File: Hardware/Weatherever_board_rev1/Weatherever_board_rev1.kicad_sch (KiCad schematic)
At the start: 44 parts, among them J101 USB_B_Micro, J102 Expansion conn, J103 DebugConn, U101 USBLC6-2P6, U102 FT230XQ, U103 AOZ1312, U104 NCP115AMX250TCG, U105 STM32G030C8T6, U106 M24C08-W, U107 M24C08-W, Y101 49S-16.000MEEJ-T 16MHz, Y102 32.768K-CFPX217

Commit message: Finished HW schematic and minor project cleanup
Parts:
- removed R108: 2k, Resistor_SMD:R_0805_2012Metric_Pad1.20x1.40mm_HandSolder, symbol Device:R_Small
- added C104: 10u, Capacitor_SMD:C_0805_2012Metric_Pad1.18x1.45mm_HandSolder, symbol Device:C_Small
- added D101: ERR_LED (RED), symbol Device:LED
- added J103: Test pins COMM1, Connector_PinHeader_2.54mm:PinHeader_2x03_P2.54mm_Vertical, symbol Connector_Generic:Conn_01x06
- added J105: Test pins Probe, Connector_PinHeader_2.54mm:PinHeader_1x02_P2.54mm_Vertical, symbol Connector_Generic:Conn_01x02
- added J106: Test pins COMM2, Connector_PinHeader_2.54mm:PinHeader_2x03_P2.54mm_Vertical, symbol Connector_Generic:Conn_01x06
- added R101, R102: 2k, Resistor_SMD:R_0805_2012Metric_Pad1.20x1.40mm_HandSolder, symbol Device:R_Small
- added R103: 270, Resistor_SMD:R_0805_2012Metric_Pad1.20x1.40mm_HandSolder, symbol Device:R_Small
- added R109, R110: 3k3, Resistor_SMD:R_0805_2012Metric_Pad1.20x1.40mm_HandSolder, symbol Device:R_Small
- added SW101: DBG - Normal, symbol Switch:SW_DIP_x01
- added SW102: RESET, symbol Switch:SW_MEC_5E
- R111: renamed from R106; value 2k -> 3k3
- R112: renamed from R107; value 2k -> 3k3
- renumbered C104 to C105, C105 to C106, C106 to C107, C107 to C108, C108 to C109, C109 to C110, C110 to C111, C111 to C112, C112 to C113, C113 to C114, C114 to C115, D101 to D102, D102 to D103, J103 to J104, R101 to R104, R102 to R105, R103 to R106, R104 to R107, R105 to R108, R109 to R113, R110 to R114
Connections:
- net +3V3: now also U106.3 (E2), R101.2, R102.1, R103.1, R109.1, R110.1
- net GNDD: now also U106.7 (WC), U107.3 (E2), U107.7 (WC), C104.2, J103.6 (Pin_6), J105.2 (Pin_2), J106.6 (Pin_6), SW101.1, SW102.1, SW102.2
- net I2C1_SCL: now also R111.2
- net I2C1_SDA: now also R112.2
- net I2C2_SCL_MEM: now also R109.2, R110.2; no longer R111.2
- net I2C2_SDA_MEM: no longer R112.2
- net SPI1_CS1: now also J103.2 (Pin_2)
- net SPI1_CS2: now also J103.1 (Pin_1)
- net SPI1_MISO: now also J103.4 (Pin_4)
- net SPI1_MOSI: now also J103.3 (Pin_3)
- net SPI1_SCK: now also J103.5 (Pin_5)
- net TIM_IN: now also J105.1 (Pin_1)
- net USART1_CTS: now also J106.4 (Pin_4)
- net USART1_RTS: now also J106.3 (Pin_3)
- net USART1_RX: now also J106.2 (Pin_2)
- net USART1_TX: now also J106.1 (Pin_1)
- net USB_D+: now also J101.3 (D+); no longer U102.6 (USBDP)
- net USB_D-: now also J101.2 (D-), U101.6 (I/O1); no longer U101.3 (I/O2), U102.7 (USBDM)
- net USB_D_S-: now reaches U101.1 (I/O1)
- net USB_D_S-: now also U102.7 (USBDM); no longer J101.2 (D-)
- net ~{RESET}: now reaches U105.10 (NRST)
- net ~{RESET}: now also C104.1, R102.2, SW102.3 (K), SW102.4 (A)
- net ~{ERR_LED}: now reaches U105.40 (PD2)
- net ~{ERR_LED}: now also D101.1 (K)
- net OVERTEMP_INT: now reaches U105.41 (PD3)
- net MODE_SEL: now reaches U105.42 (PB3)
- net MODE_SEL: now also R101.1, SW101.2
- new net: D101.2 (A), R103.2
- new net USB_D_S+: U101.3 (I/O2), U102.6 (USBDP)
- no-connect marks 22 -> 20
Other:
- added sheet OnBoardThermometer (OnBoardThermometer.kicad_sch)
- note added: "Device I^{2}C address: 0x50"
- note added: "Device I^{2}C address: 0x54"
- note added: "Error indicator LED and RESET button"
- note added: "Mode select switch"
- note added: "SW ON -> Debug SW OFF -> Normal"
- note added: "The _S suffix is for "Safe" (from ESD threats :))"
- moved on the sheet: C109, J101, J102, R111, R112, U101, U106

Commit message: Funished schematics and GPIO drv interface
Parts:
- removed R113, R114: 10k, Resistor_SMD:R_0805_2012Metric_Pad1.20x1.40mm_HandSolder, symbol Device:R_Small
- added J107: Test pins I2C, Connector_PinHeader_2.54mm:PinHeader_2x03_P2.54mm_Vertical, symbol Connector_Generic:Conn_01x06
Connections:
- net GNDD: now also J107.3 (Pin_3), J107.4 (Pin_4)
- net I2C1_SCL: now also J107.5 (Pin_5)
- net I2C1_SDA: now also J107.6 (Pin_6)
- net I2C2_SCL_MEM: now also J107.1 (Pin_1)
- net I2C2_SDA_MEM: now also J107.2 (Pin_2)
- net RF_DIO_2: now reaches U105.23 (PB11)
- net RF_DIO_3: now reaches U105.24 (PB12)
- net RF_DIO_5: now reaches U105.43 (PB4)
- net RF_DIO_4: now reaches U105.44 (PB5)
- net OVERTEMP_INT renamed PRS_RDY
- net RF_GDO0 renamed RF_DIO_0
- net RF_GDO2 renamed RF_DIO_1
- no-connect marks 20 -> 16
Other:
- sheet OnBoardThermometer renamed EvnSensors
- added sheet USB_Dongle (USB_Dongle.kicad_sch)
- sheet EvnSensors ports: added PREASURE_IRQ, SCL_SENS, SDA_SENS; removed OVERTEMP_THM, SCL_THM, SDA_THM
- sheet RadioComm ports: added RF_DIO0, RF_DIO1, RF_DIO2, RF_DIO3, RF_DIO4, RF_DIO5, RF_RESET; removed RF_GDO0, RF_GDO2
- moved on the sheet: J105

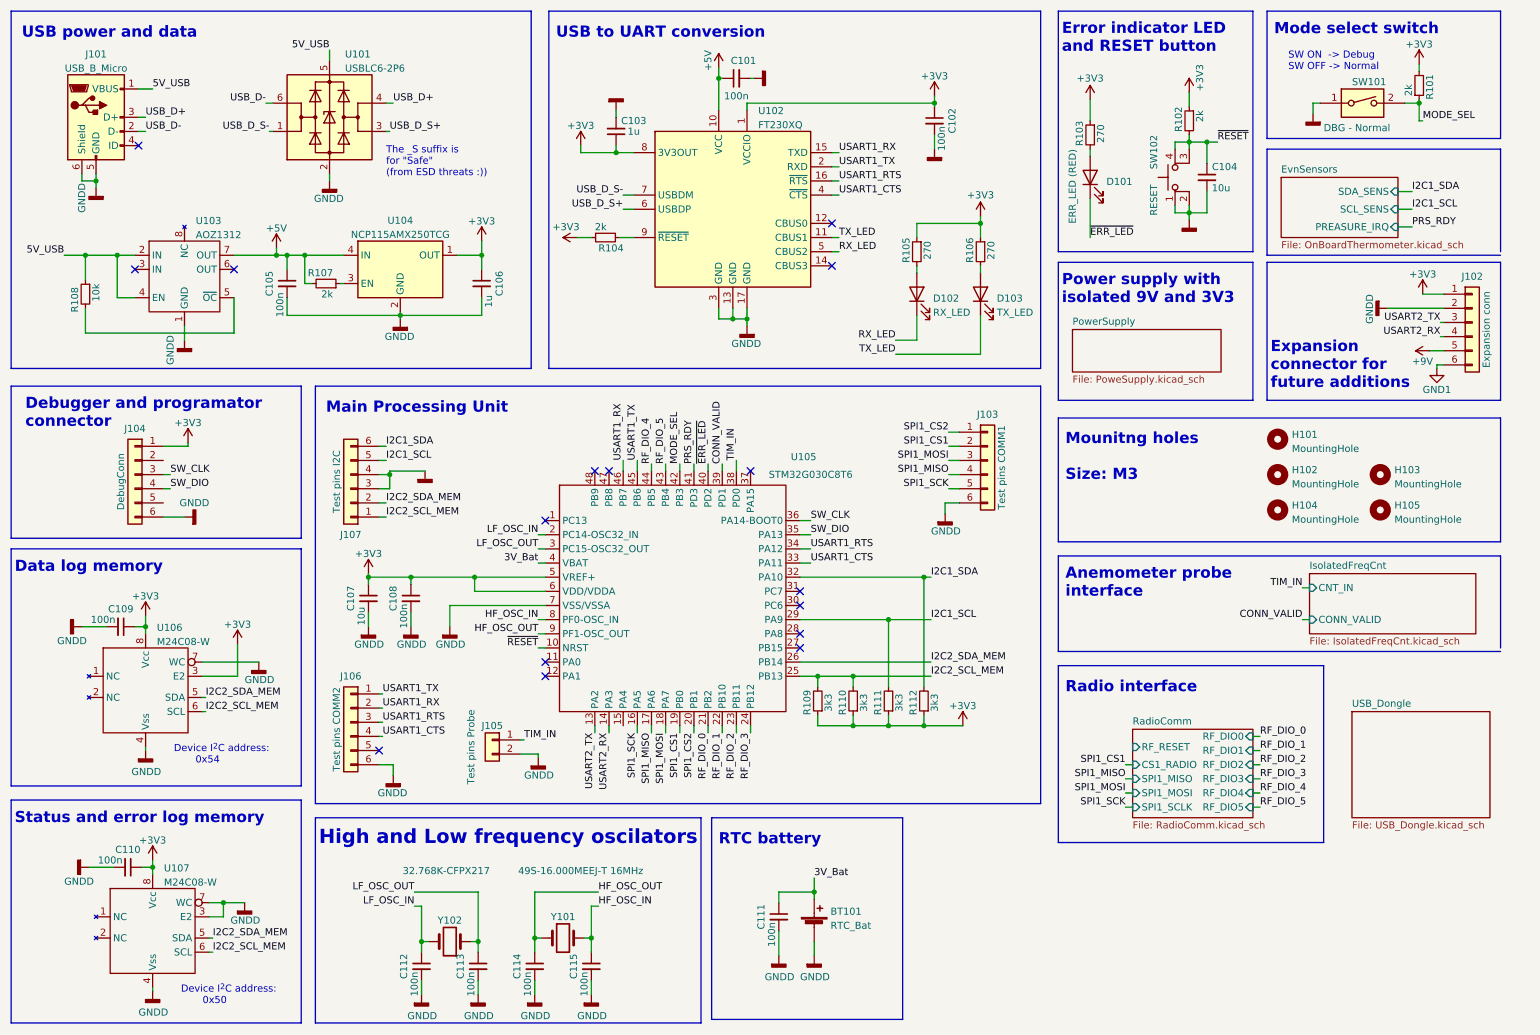
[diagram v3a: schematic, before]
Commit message: Some components footprint updates
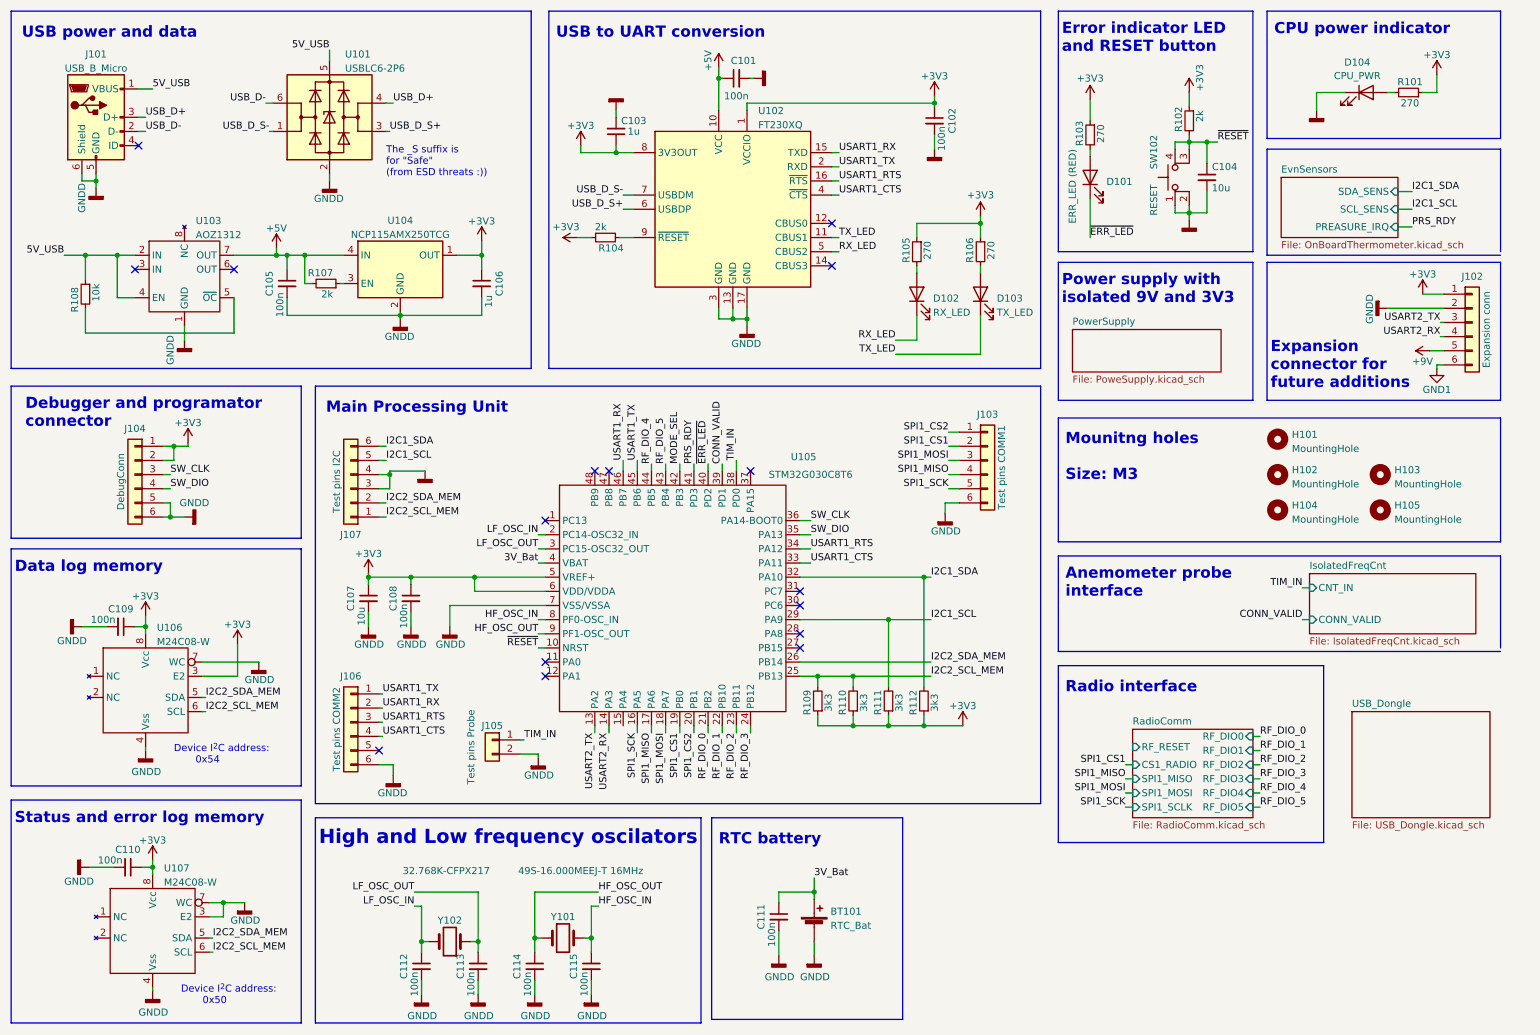
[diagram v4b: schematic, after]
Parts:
- removed SW101: DBG - Normal, symbol Switch:SW_DIP_x01
- added D104: CPU_PWR, Diode_SMD:D_0805_2012Metric_Pad1.15x1.40mm_HandSolder, symbol Device:LED
- D101, D102, D103: footprint (none) -> Diode_SMD:D_0805_2012Metric_Pad1.15x1.40mm_HandSolder
- R101: value 2k -> 270
- SW102: footprint (none) -> Button_Switch_SMD:SW_Push_1P1T_NO_6x6mm_H9.5mm
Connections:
- net +3V3: now also J104.2 (Pin_2), R101.1; no longer R101.2
- net GNDD: now also J104.5 (Pin_5), D104.1 (K)
- net MODE_SEL: no longer R101.1
- new net: D104.2 (A), R101.2
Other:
- note added: "CPU power indicator"
- note removed: "Mode select switch"
- note removed: "SW ON -> Debug SW OFF -> Normal"

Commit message: Layout impl start
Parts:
- C101, C102: footprint Capacitor_SMD:C_0805_2012Metric_Pad1.18x1.45mm_HandSolder -> Capacitor_SMD:C_0402_1005Metric_Pad0.74x0.62mm_HandSolder
- C105: footprint Capacitor_SMD:C_0805_2012Metric_Pad1.18x1.45mm_HandSolder -> Capacitor_SMD:C_0504_1310Metric_Pad0.83x1.28mm_HandSolder
- R104, R107, R108: footprint Resistor_SMD:R_0805_2012Metric_Pad1.20x1.40mm_HandSolder -> Resistor_SMD:R_0402_1005Metric_Pad0.72x0.64mm_HandSolder
- SW102: symbol Switch:SW_MEC_5E -> Switch:SW_Push
- Y101: value 49S-16.000MEEJ-T 16MHz -> 3225-16M-SR 16MHz 9pF; footprint (none) -> Crystal:Crystal_SMD_TXC_7M-4Pin_3.2x2.5mm_HandSoldering; symbol Device:Crystal -> Device:Crystal_GND24
- Y102: footprint (none) -> Crystal:Crystal_SMD_TXC_7A-2Pin_5x3.2mm
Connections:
- net GNDD: now also Y101.2, Y101.4; no longer SW102.2
- net HF_OSC_IN: now also Y101.3; no longer Y101.2
- net USB_D+: now also U101.3 (I/O2); no longer U101.4 (I/O2)
- net USB_D-: now also U101.1 (I/O1); no longer U101.6 (I/O1)
- net USB_D_S+: now also U101.4 (I/O2); no longer U101.3 (I/O2)
- net USB_D_S-: now also U101.6 (I/O1); no longer U101.1 (I/O1)
- net ~{RESET}: now also SW102.2; no longer SW102.3 (K), SW102.4 (A)
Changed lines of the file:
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@@
   (junction (at 141.605 26.67) (diameter 0) (color 0 0 0 0)
   )
+  (junction (at 118.745 189.865) (diameter 0) (color 0 0 0 0)
+  )
   (junction (at 165.735 142.875) (diameter 0) (color 0 0 0 0)
   )
@@
     (stroke (width 0) (type default))
   )
-  (wire (pts (xy 223.52 49.53) (xy 223.52 50.8))
-    (stroke (width 0) (type default))
-  )
   (wire (pts (xy 214.63 154.94) (xy 215.9 154.94))
     (stroke (width 0) (type default))
@@
     (stroke (width 0) (type default))
   )
+  (wire (pts (xy 121.92 175.895) (xy 121.92 189.865))
+    (stroke (width 0) (type default))
+  )
   (wire (pts (xy 226.06 49.53) (xy 226.06 50.8))
     (stroke (width 0) (type default))
@@
     (stroke (width 0) (type default))
   )
+  (wire (pts (xy 118.745 189.865) (xy 118.745 191.135))
+    (stroke (width 0) (type default))
+  )
   (wire (pts (xy 147.32 142.875) (xy 147.32 144.145))
     (stroke (width 0) (type default))
@@
     (stroke (width 0) (type default))
   )
-  (wire (pts (xy 60.325 31.115) (xy 61.595 31.115))
+  (wire (pts (xy 60.96 31.115) (xy 61.595 31.115))
     (stroke (width 0) (type default))
   )
@@
     (stroke (width 0) (type default))
   )
-  (wire (pts (xy 223.52 39.37) (xy 223.52 38.1))
-    (stroke (width 0) (type default))
-  )
   (wire (pts (xy 41.91 102.87) (xy 43.18 102.87))
     (stroke (width 0) (type default))
@@
     (stroke (width 0) (type default))
   )
-  (wire (pts (xy 82.55 36.195) (xy 81.915 36.195))
+  (wire (pts (xy 83.185 36.195) (xy 81.915 36.195))
     (stroke (width 0) (type default))
   )
@@
     (stroke (width 0) (type default))
   )
+  (wire (pts (xy 113.665 189.865) (xy 118.745 189.865))
+    (stroke (width 0) (type default))
+  )
   (wire (pts (xy 147.32 26.67) (xy 147.955 26.67))
     (stroke (width 0) (type default))
@@
     (stroke (width 0) (type default))
   )
+  (wire (pts (xy 113.665 186.055) (xy 113.665 189.865))
+    (stroke (width 0) (type default))
+  )
   (wire (pts (xy 41.91 105.41) (xy 43.18 105.41))
     (stroke (width 0) (type default))
@@
     (stroke (width 0) (type default))
   )
+  (wire (pts (xy 121.92 189.865) (xy 118.745 189.865))
+    (stroke (width 0) (type default))
+  )
   (wire (pts (xy 83.185 31.115) (xy 81.915 31.115))
     (stroke (width 0) (type default))
@@
     (stroke (width 0) (type default))
   )
+  (wire (pts (xy 113.665 175.895) (xy 121.92 175.895))
+    (stroke (width 0) (type default))
+  )
   (wire (pts (xy 78.74 117.475) (xy 78.74 116.205))
     (stroke (width 0) (type default))
@@
     (stroke (width 0) (type default))
   )
-  (wire (pts (xy 223.52 50.8) (xy 226.06 50.8))
-    (stroke (width 0) (type default))
-  )
   (wire (pts (xy 81.915 105.41) (xy 80.645 105.41))
     (stroke (width 0) (type default))
@@
     (stroke (width 0) (type default))
   )
-  (wire (pts (xy 223.52 38.1) (xy 226.06 38.1))
-    (stroke (width 0) (type default))
-  )
   (wire (pts (xy 142.24 26.67) (xy 141.605 26.67))
     (stroke (width 0) (type default))
@@
     (stroke (width 0) (type default))
   )
-  (wire (pts (xy 118.745 188.595) (xy 118.745 191.135))
+  (wire (pts (xy 118.745 188.595) (xy 118.745 189.865))
     (stroke (width 0) (type default))
   )
@@
     (effects (font (size 1.27 1.27)) (justify left bottom))
   )
-  (label "USB_D-" (at 60.325 31.115 180) (fields_autoplaced)
+  (label "USB_D-" (at 60.96 36.195 180) (fields_autoplaced)
     (effects (font (size 1.27 1.27)) (justify right bottom))
   )
@@
     (effects (font (size 1.27 1.27)) (justify right bottom))
   )
-  (label "USB_D_S+" (at 82.55 36.195 0) (fields_autoplaced)
+  (label "USB_D_S+" (at 83.185 31.115 0) (fields_autoplaced)
     (effects (font (size 1.27 1.27)) (justify left bottom))
   )
@@
     (effects (font (size 1.27 1.27)) (justify right bottom))
   )
-  (label "USB_D_S-" (at 60.96 36.195 180) (fields_autoplaced)
+  (label "USB_D_S-" (at 60.96 31.115 180) (fields_autoplaced)
     (effects (font (size 1.27 1.27)) (justify right bottom))
   )
@@
     (effects (font (size 1.27 1.27)) (justify left bottom))
   )
-  (label "USB_D+" (at 83.185 31.115 0) (fields_autoplaced)
+  (label "USB_D+" (at 83.185 36.195 0) (fields_autoplaced)
     (effects (font (size 1.27 1.27)) (justify left bottom))
   )
@@
       (effects (font (size 1.27 1.27)) (justify right))
     )
-    (property "Footprint" "Resistor_SMD:R_0805_2012Metric_Pad1.20x1.40mm_HandSolder" (at 121.285 55.245 0)
+    (property "Footprint" "Resistor_SMD:R_0402_1005Metric_Pad0.72x0.64mm_HandSolder" (at 121.285 55.245 0)
       (effects (font (size 1.27 1.27)) hide)
     )
@@
     )
   )
-  (symbol (lib_id "Switch:SW_MEC_5E") (at 226.06 44.45 90) (unit 1)
+  (symbol (lib_id "Switch:SW_Push") (at 226.06 44.45 90) (unit 1)
     (in_bom yes) (on_board yes) (dnp no)
-    (property "Reference" "SW102" (at 219.71 36.83 0)
+    (property "Reference" "SW102" (at 220.98 36.83 0)
       (effects (font (size 1.27 1.27)) (justify right))
     )
-    (property "Value" "RESET" (at 219.71 45.72 0)
+    (property "Value" "RESET" (at 221.615 45.72 0)
       (effects (font (size 1.27 1.27)) (justify right))
     )
-    (property "Footprint" "Button_Switch_SMD:SW_Push_1P1T_NO_6x6mm_H9.5mm" (at 218.44 44.45 0)
+    (property "Footprint" "Button_Switch_SMD:SW_Push_1P1T_NO_6x6mm_H9.5mm" (at 220.98 44.45 0)
       (effects (font (size 1.27 1.27)) hide)
     )
-    (property "Datasheet" "http://www.apem.com/int/index.php?controller=attachment&id_attachment=1371" (at 218.44 44.45 0)
+    (property "Datasheet" "~" (at 220.98 44.45 0)
       (effects (font (size 1.27 1.27)) hide)
     )
     (pin "1")
     (pin "2")
-    (pin "3")
-    (pin "4")
     (instances
       (project "Weatherever_board_rev1"
@@
       (effects (font (size 1.27 1.27)))
     )
-    (property "Footprint" "Capacitor_SMD:C_0805_2012Metric_Pad1.18x1.45mm_HandSolder" (at 64.135 63.5 0)
+    (property "Footprint" "Capacitor_SMD:C_0504_1310Metric_Pad0.83x1.28mm_HandSolder" (at 64.135 63.5 0)
       (effects (font (size 1.27 1.27)) hide)
     )
@@
       (effects (font (size 1.27 1.27)) (justify right))
     )
-    (property "Footprint" "Resistor_SMD:R_0805_2012Metric_Pad1.20x1.40mm_HandSolder" (at 27.94 65.405 0)
+    (property "Footprint" "Resistor_SMD:R_0402_1005Metric_Pad0.72x0.64mm_HandSolder" (at 27.94 65.405 0)
       (effects (font (size 1.27 1.27)) hide)
     )
@@
       (effects (font (size 1.27 1.27)))
     )
-    (property "Footprint" "" (at 93.345 181.61 0)
+    (property "Footprint" "Crystal:Crystal_SMD_TXC_7A-2Pin_5x3.2mm" (at 93.345 181.61 0)
       (effects (font (size 1.27 1.27)) hide)
     )
@@
     )
   )
-  (symbol (lib_id "Device:Crystal") (at 113.665 180.975 0) (unit 1)
+  (symbol (lib_id "Device:Crystal_GND24") (at 113.665 180.975 0) (unit 1)
     (in_bom yes) (on_board yes) (dnp no)
-    (property "Reference" "Y101" (at 113.665 177.165 0)
+    (property "Reference" "Y101" (at 113.665 173.99 0)
       (effects (font (size 1.27 1.27)))
     )
-    (property "Value" "49S-16.000MEEJ-T 16MHz" (at 116.84 168.91 0)
+    (property "Value" "3225-16M-SR 16MHz 9pF" (at 116.84 168.91 0)
       (effects (font (size 1.27 1.27)))
     )
-    (property "Footprint" "" (at 113.665 180.975 0)
+    (property "Footprint" "Crystal:Crystal_SMD_TXC_7M-4Pin_3.2x2.5mm_HandSoldering" (at 113.665 180.975 0)
       (effects (font (size 1.27 1.27)) hide)
     )
@@
     (pin "1")
     (pin "2")
+    (pin "3")
+    (pin "4")
     (instances
       (project "Weatherever_board_rev1"
@@
       (effects (font (size 1.27 1.27)) (justify right))
     )
-    (property "Footprint" "Resistor_SMD:R_0805_2012Metric_Pad1.20x1.40mm_HandSolder" (at 71.12 63.5 0)
+    (property "Footprint" "Resistor_SMD:R_0402_1005Metric_Pad0.72x0.64mm_HandSolder" (at 71.12 63.5 0)
       (effects (font (size 1.27 1.27)) hide)
     )
@@
       (effects (font (size 1.27 1.27)))
     )
-    (property "Footprint" "Capacitor_SMD:C_0805_2012Metric_Pad1.18x1.45mm_HandSolder" (at 180.34 34.29 0)
+    (property "Footprint" "Capacitor_SMD:C_0402_1005Metric_Pad0.74x0.62mm_HandSolder" (at 180.34 34.29 0)
       (effects (font (size 1.27 1.27)) hide)
     )
@@
       (effects (font (size 1.27 1.27)))
     )
-    (property "Footprint" "Capacitor_SMD:C_0805_2012Metric_Pad1.18x1.45mm_HandSolder" (at 144.78 26.67 0)
+    (property "Footprint" "Capacitor_SMD:C_0402_1005Metric_Pad0.74x0.62mm_HandSolder" (at 144.78 26.67 0)
       (effects (font (size 1.27 1.27)) hide)
     )
